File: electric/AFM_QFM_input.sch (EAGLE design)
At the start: 31 parts, among them U1 AD9833BRM, U2 LM339D, U3 LM324KAD, U4 SN74LVC1G86DCKRG4, Y1 OSCILLATORSMD-5X3

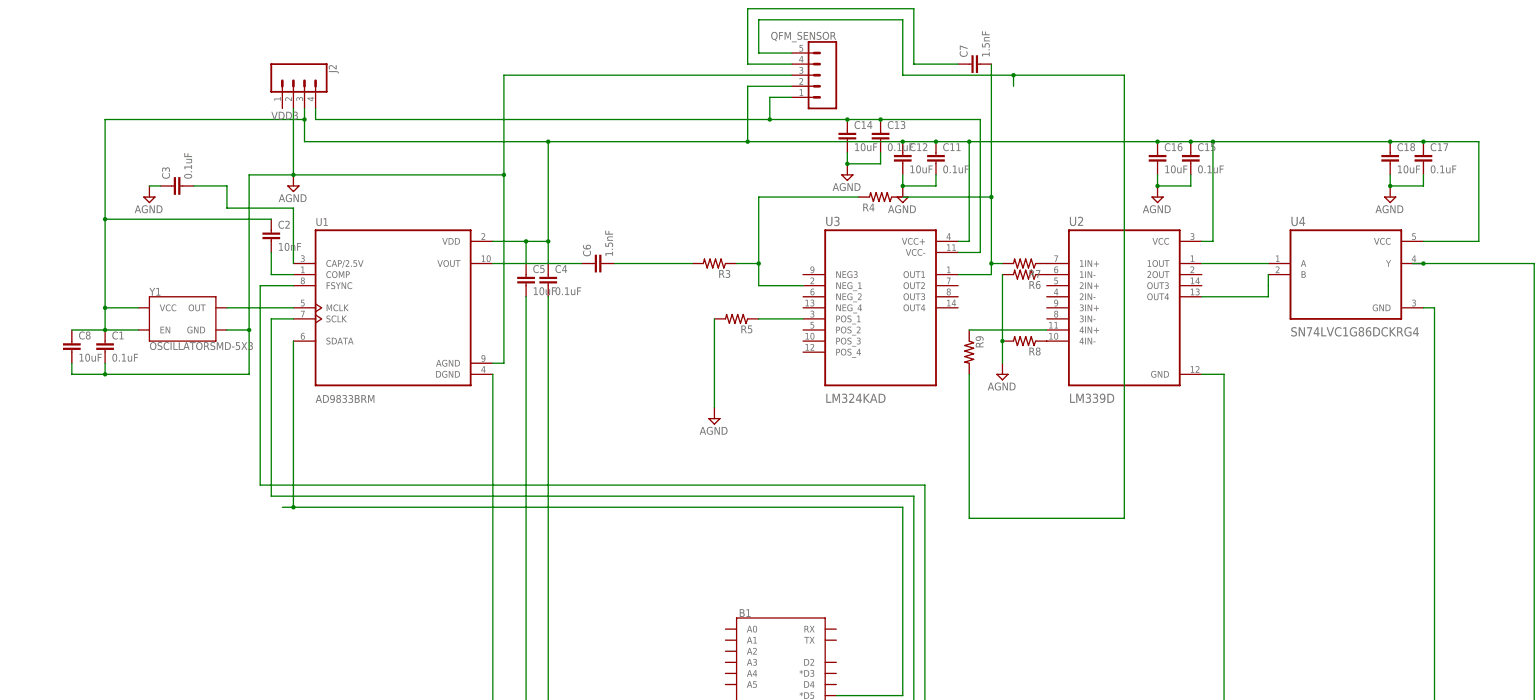
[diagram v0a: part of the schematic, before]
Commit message: Updated to boards. Changes reflects fixes needed to PCBWay boards
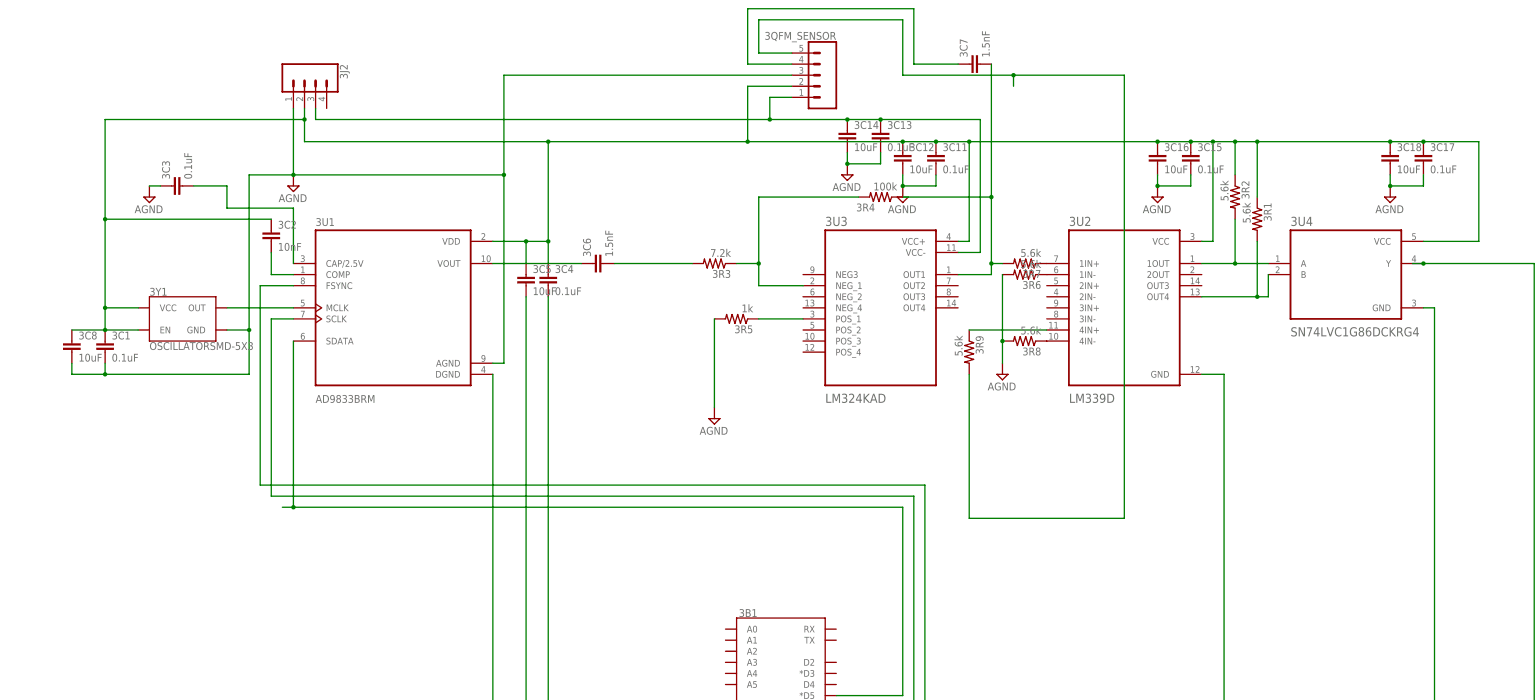
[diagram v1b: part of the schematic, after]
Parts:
- removed J2: (no value), SparkFun-Connectors:CONN_04LONGPADS
- added 3J2: (no value), SparkFun-Connectors:CONN_04LONGPADS
- added 3R1, 3R2: 5.6k, rcl:R-US_R0603
- 3R3: value (none) -> 7.2k
- 3R4: value (none) -> 100k
- 3R5: value (none) -> 1k
- 3R6, 3R7, 3R8, 3R9: value (none) -> 5.6k
- renumbered B1 to 3B1, C1 to 3C1, C11 to 3C11, C12 to 3C12, C13 to 3C13, C14 to 3C14, C15 to 3C15, C16 to 3C16, C17 to 3C17, C18 to 3C18, C2 to 3C2, C3 to 3C3, C4 to 3C4, C5 to 3C5, C6 to 3C6, C7 to 3C7, C8 to 3C8, QFM_SENSOR to 3QFM_SENSOR, R3 to 3R3, R4 to 3R4, R5 to 3R5, R6 to 3R6, R7 to 3R7, R8 to 3R8, R9 to 3R9, U1 to 3U1, U2 to 3U2, U3 to 3U3, U4 to 3U4, Y1 to 3Y1
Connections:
- net AGND: now also 3J2.1; no longer J2.2
- net N$16: now also 3R2.2
- net N$21: now also 3R1.2
- net VCC: now also 3J2.3; no longer J2.4
- net VDD3: now also 3J2.2, 3R1.1, 3R2.1; no longer J2.3
